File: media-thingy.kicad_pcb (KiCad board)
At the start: 2 copper layers, 7 parts, among them J1 Conn_02x20_Odd_Even, J2 Conn_01x04, SW1 Switch, SW2 Switch, SW3 Switch, SW4 Switch, SW5 Switch

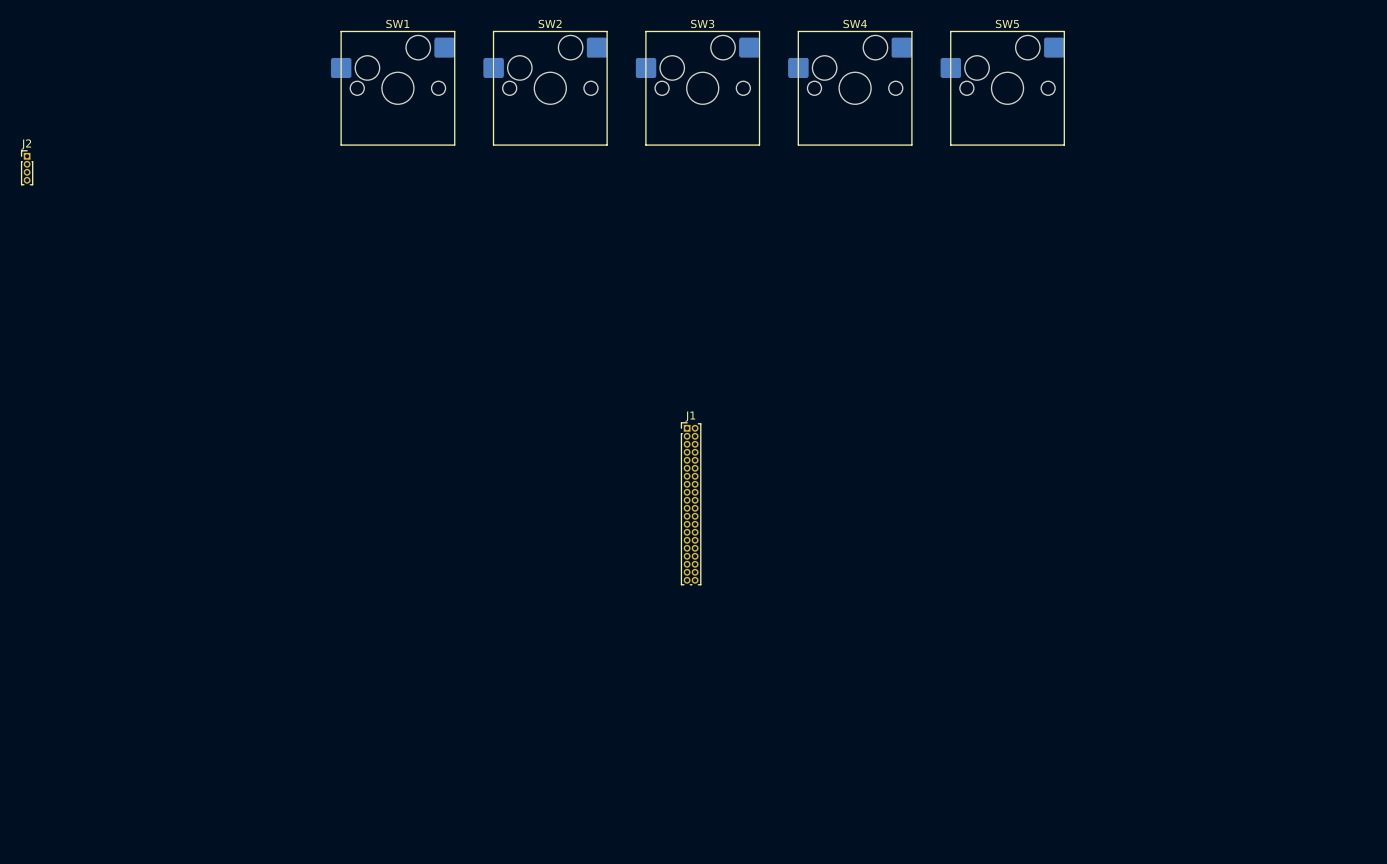
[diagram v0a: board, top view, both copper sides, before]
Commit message: correct header sizes
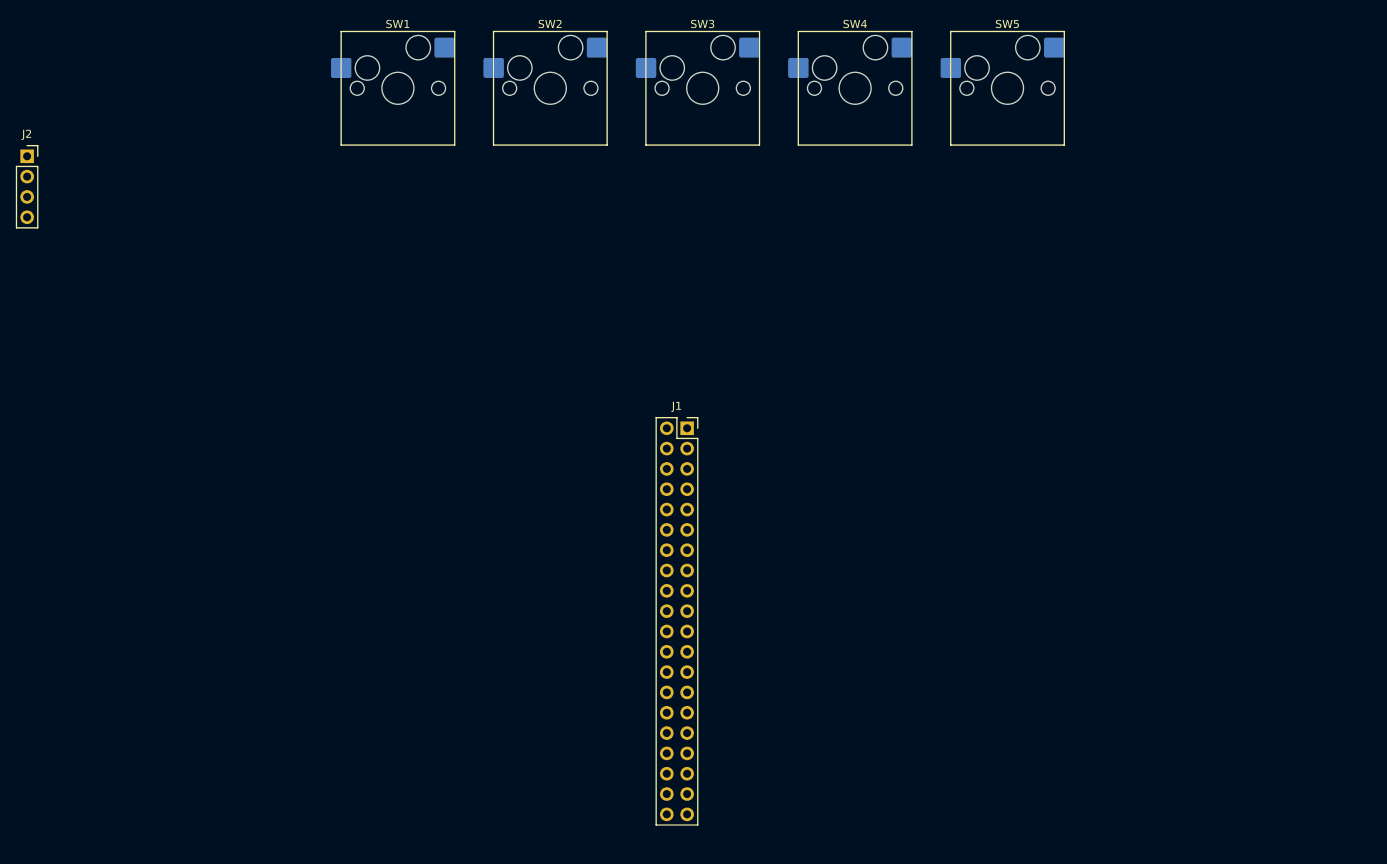
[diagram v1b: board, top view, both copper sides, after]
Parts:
- J1: footprint Connector_PinHeader_1.00mm:PinHeader_2x20_P1.00mm_Vertical -> Connector_PinSocket_2.54mm:PinSocket_2x20_P2.54mm_Vertical
- J2: footprint Connector_PinHeader_1.00mm:PinHeader_1x04_P1.00mm_Vertical -> Connector_PinSocket_2.54mm:PinSocket_1x04_P2.54mm_Vertical

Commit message: complete pcb
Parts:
- moved J2 99.0 mm to (82.5, 121.8), turned to 180 degrees
- moved SW5 66.3 mm to (175.1, 94.2)
- moved SW4 63.4 mm to (149.7, 94.2)
- moved SW3 61.1 mm to (124.3, 94.2)
- moved SW2 59.3 mm to (98.9, 94.2)
- moved SW1 58.2 mm to (73.5, 94.2)
- moved J1 28.1 mm to (99.1, 106.9), turned to 90 degrees
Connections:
- J1 pad 36: GPIO 16 -> unconnected-(J1-Pin_36-Pad36)
- J1 pad 4: +5V -> unconnected-(J1-Pin_4-Pad4)
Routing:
- net GND: track 0.00 -> 245.9 mm, vias 0 -> 1
- net GPIO 24: track 0.00 -> 61.0 mm
- net GPIO 17: track 0.00 -> 57.4 mm
- net GPIO 23: track 0.00 -> 39.3 mm
- net GPIO 27: track 0.00 -> 35.2 mm
- net LCD_CLK: track 0.00 -> 31.0 mm
- net LCD_DATA: track 0.00 -> 29.7 mm
- net +5V: track 0.00 -> 23.4 mm
- net GPIO 22: track 0.00 -> 15.2 mm
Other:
- board outline added: 128 x 52.5 mm
- board text added: "5v"
- board text added: "GND"
- board text added: "LCD_CLK"
- board text added: "LCD_DATA"

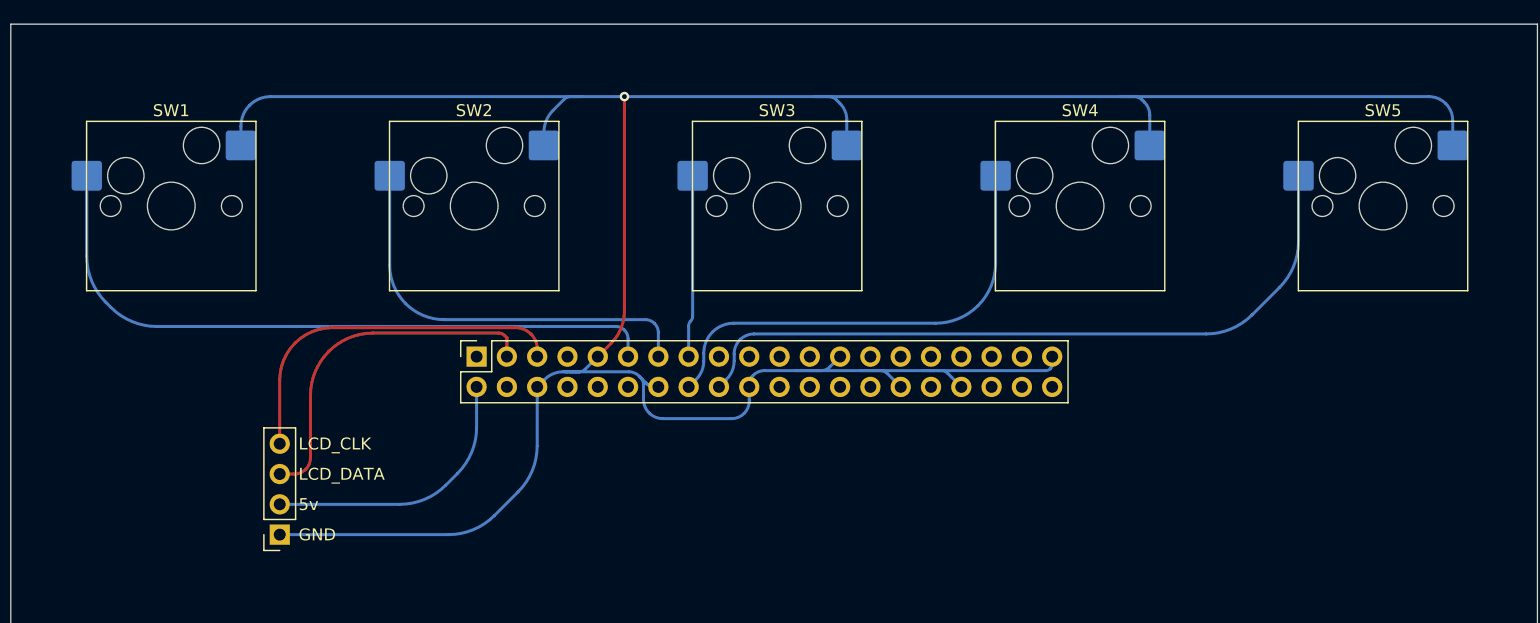
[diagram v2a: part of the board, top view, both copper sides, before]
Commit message: fix distance between switches and edge
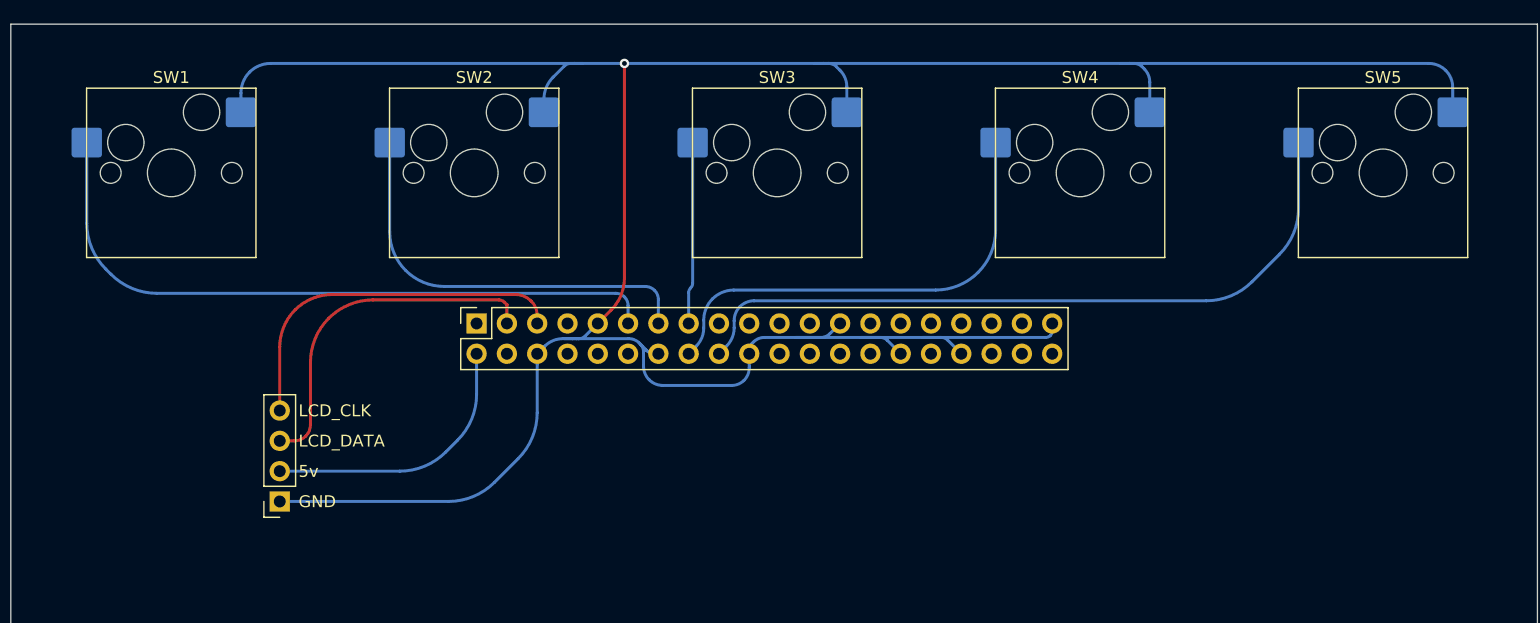
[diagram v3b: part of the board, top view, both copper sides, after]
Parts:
- moved J1 2.78 mm to (99.1, 104.1)
- moved J2 2.78 mm to (82.5, 119.0)
- moved SW1 2.78 mm to (73.5, 91.5)
- moved SW2 2.78 mm to (98.9, 91.5)
- moved SW3 2.78 mm to (124.3, 91.5)
- moved SW4 2.78 mm to (149.7, 91.5)
- moved SW5 2.78 mm to (175.1, 91.5)
